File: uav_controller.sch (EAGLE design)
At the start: 20 parts, among them IC1 PIC16F877SO, U1 L298, U2 L298, U3 LCD-16X28X2

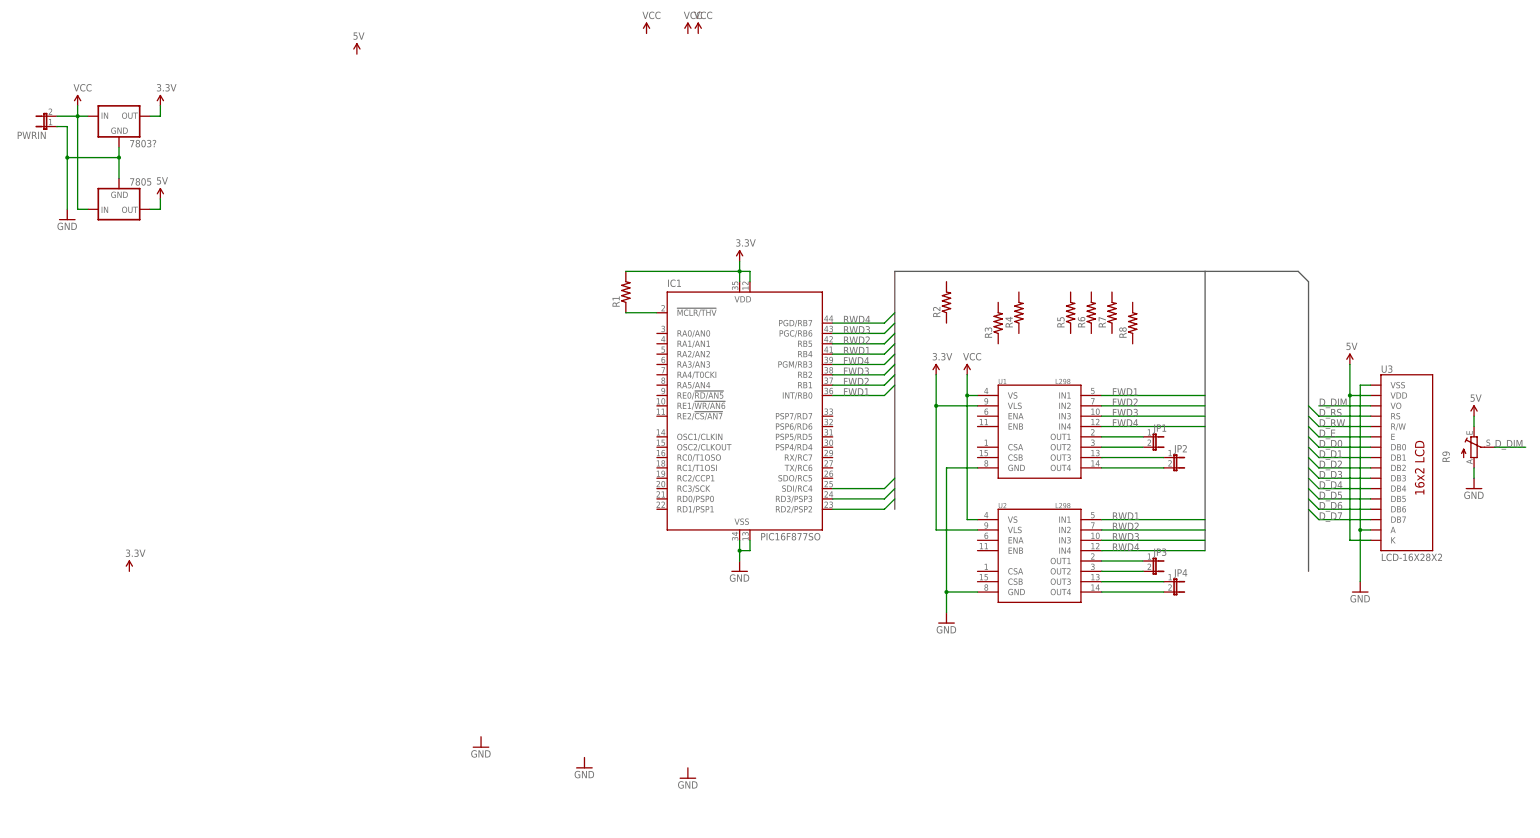
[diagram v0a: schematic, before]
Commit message: Added L3G4200D 3-Axis Gyro Carrier, not using the internal vreg. http://www.pololu.com/catalog/product/1272
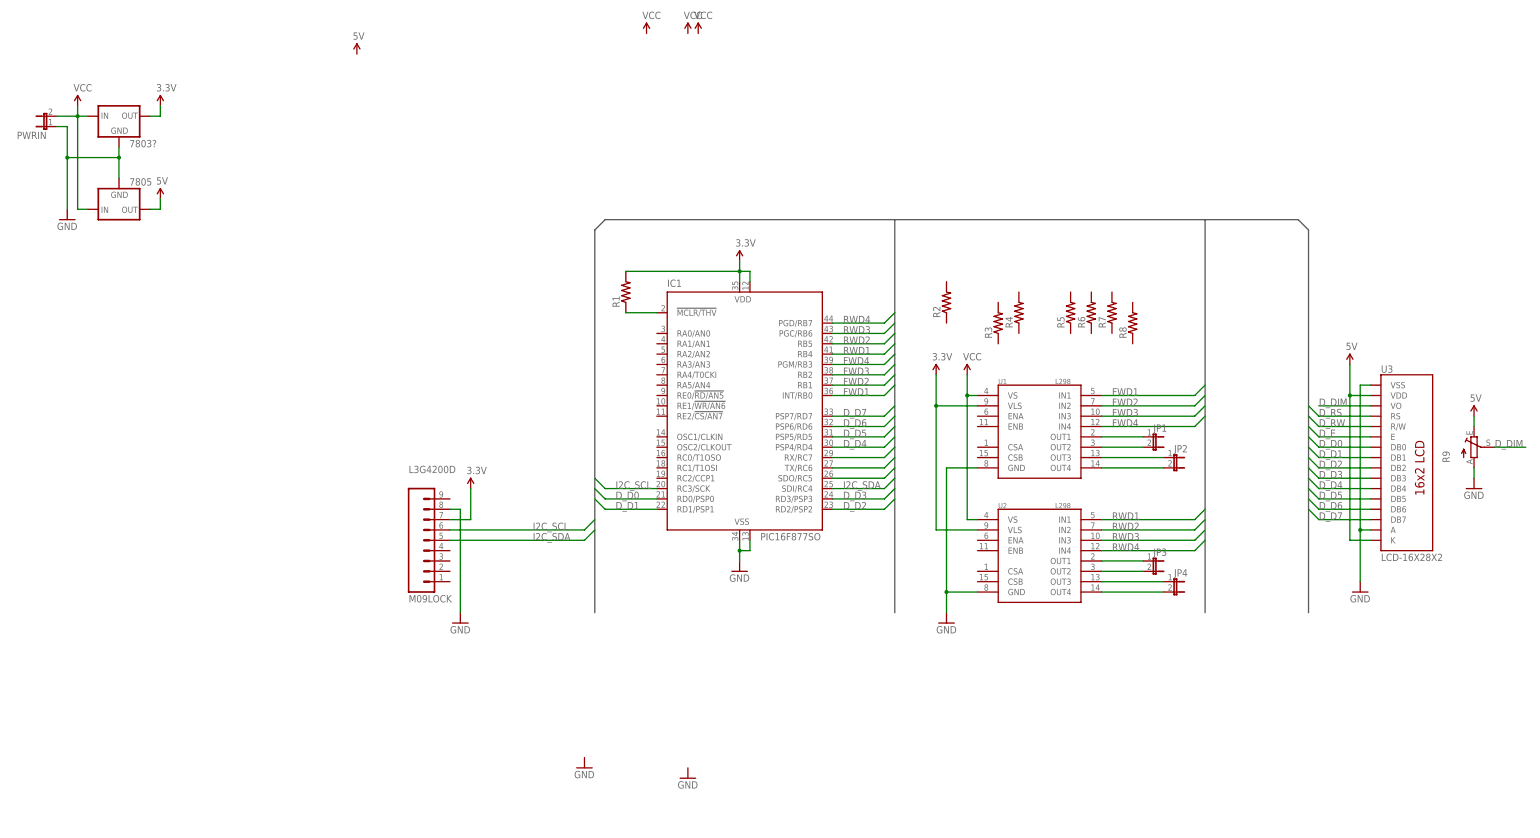
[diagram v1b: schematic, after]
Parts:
- added L3G4200D: M09LOCK, SparkFun-Connectors:M09LOCK
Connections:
- removed net N$19: IC1.RD2/PSP2
- removed net N$20: IC1.RD3/PSP3
- removed net N$21: IC1.SDI/RC4
- new net I2C_SCL: IC1.RC3/SCK, L3G4200D.6
- new net I2C_SDA: IC1.SDI/RC4, L3G4200D.5
- new net N$10: IC1.SDO/RC5
- new net N$11: IC1.TX/RC6
- new net N$12: IC1.RX/RC7
- net 3.3V: now also L3G4200D.7
- net D_D0: now also IC1.RD0/PSP0
- net D_D1: now also IC1.RD1/PSP1
- net D_D2: now also IC1.RD2/PSP2
- net D_D3: now also IC1.RD3/PSP3
- net D_D4: now also IC1.PSP4/RD4
- net D_D5: now also IC1.PSP5/RD5
- net D_D6: now also IC1.PSP6/RD6
- net D_D7: now also IC1.PSP7/RD7
- net GND: now also L3G4200D.8

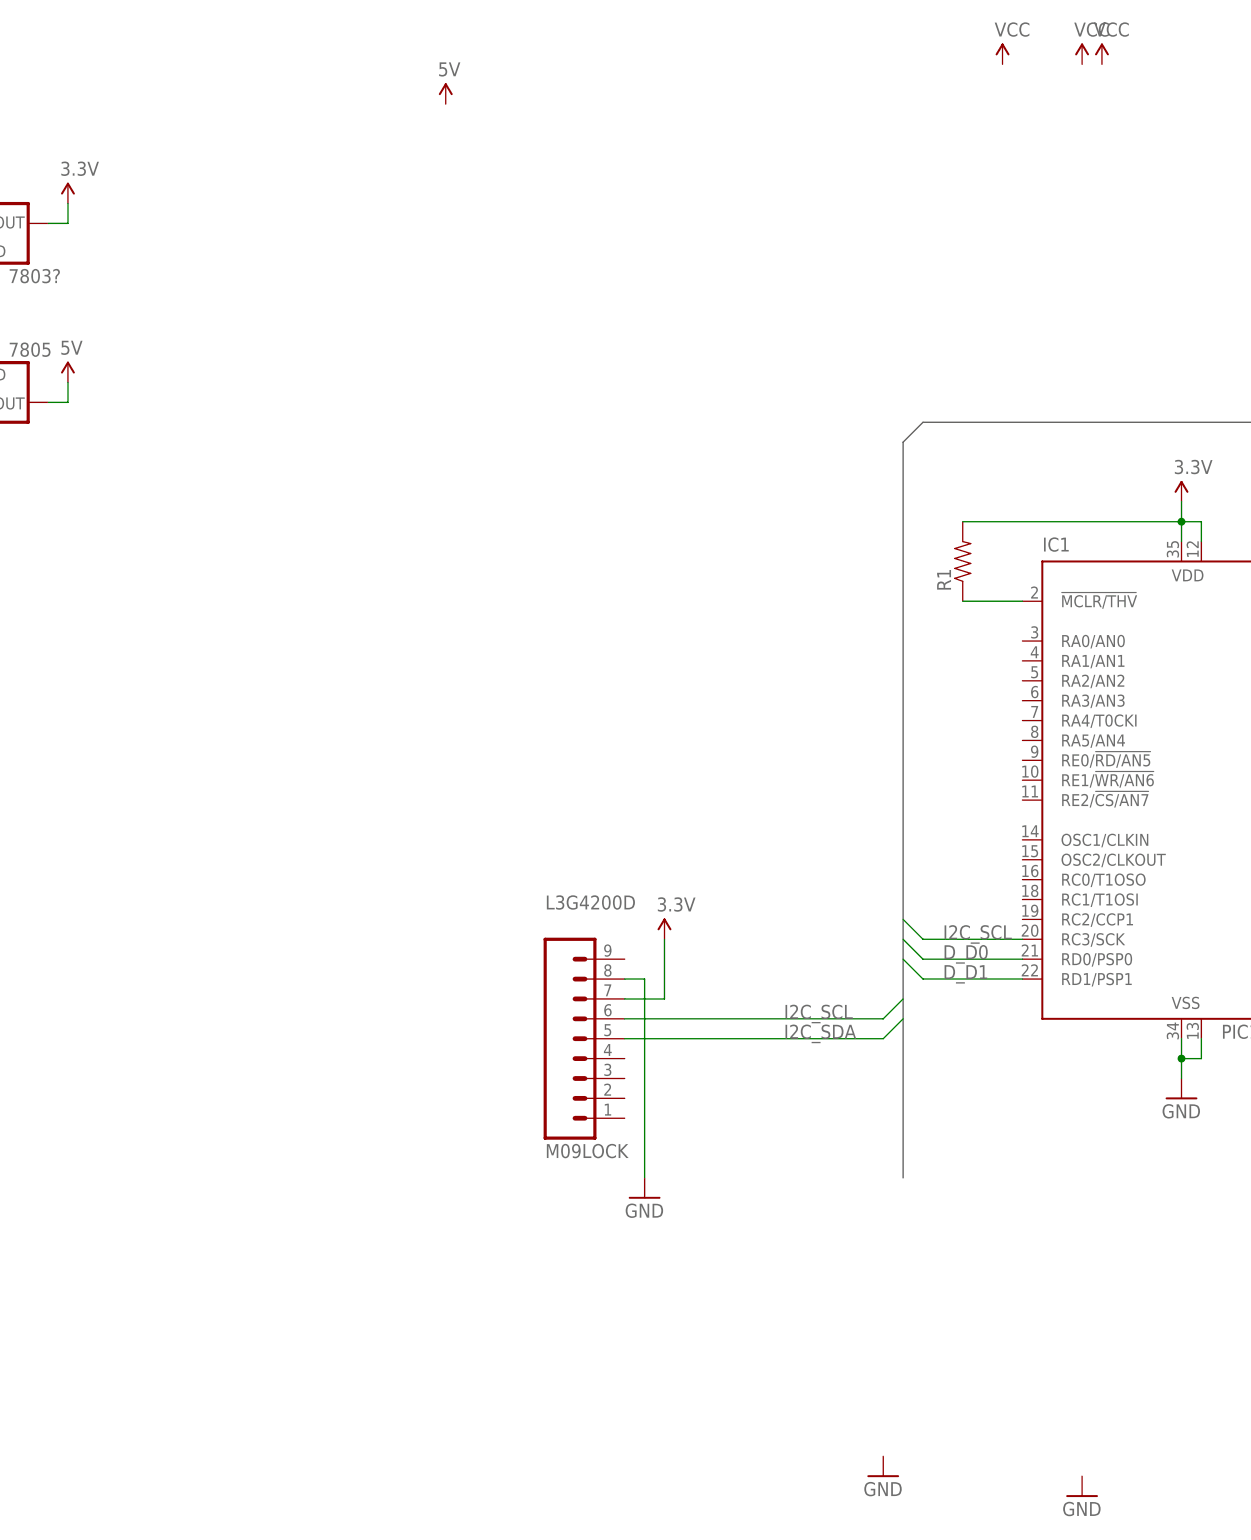
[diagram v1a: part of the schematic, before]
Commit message: Added OSC and connectors for analog range finders: http://www.pololu.com/catalog/product/136
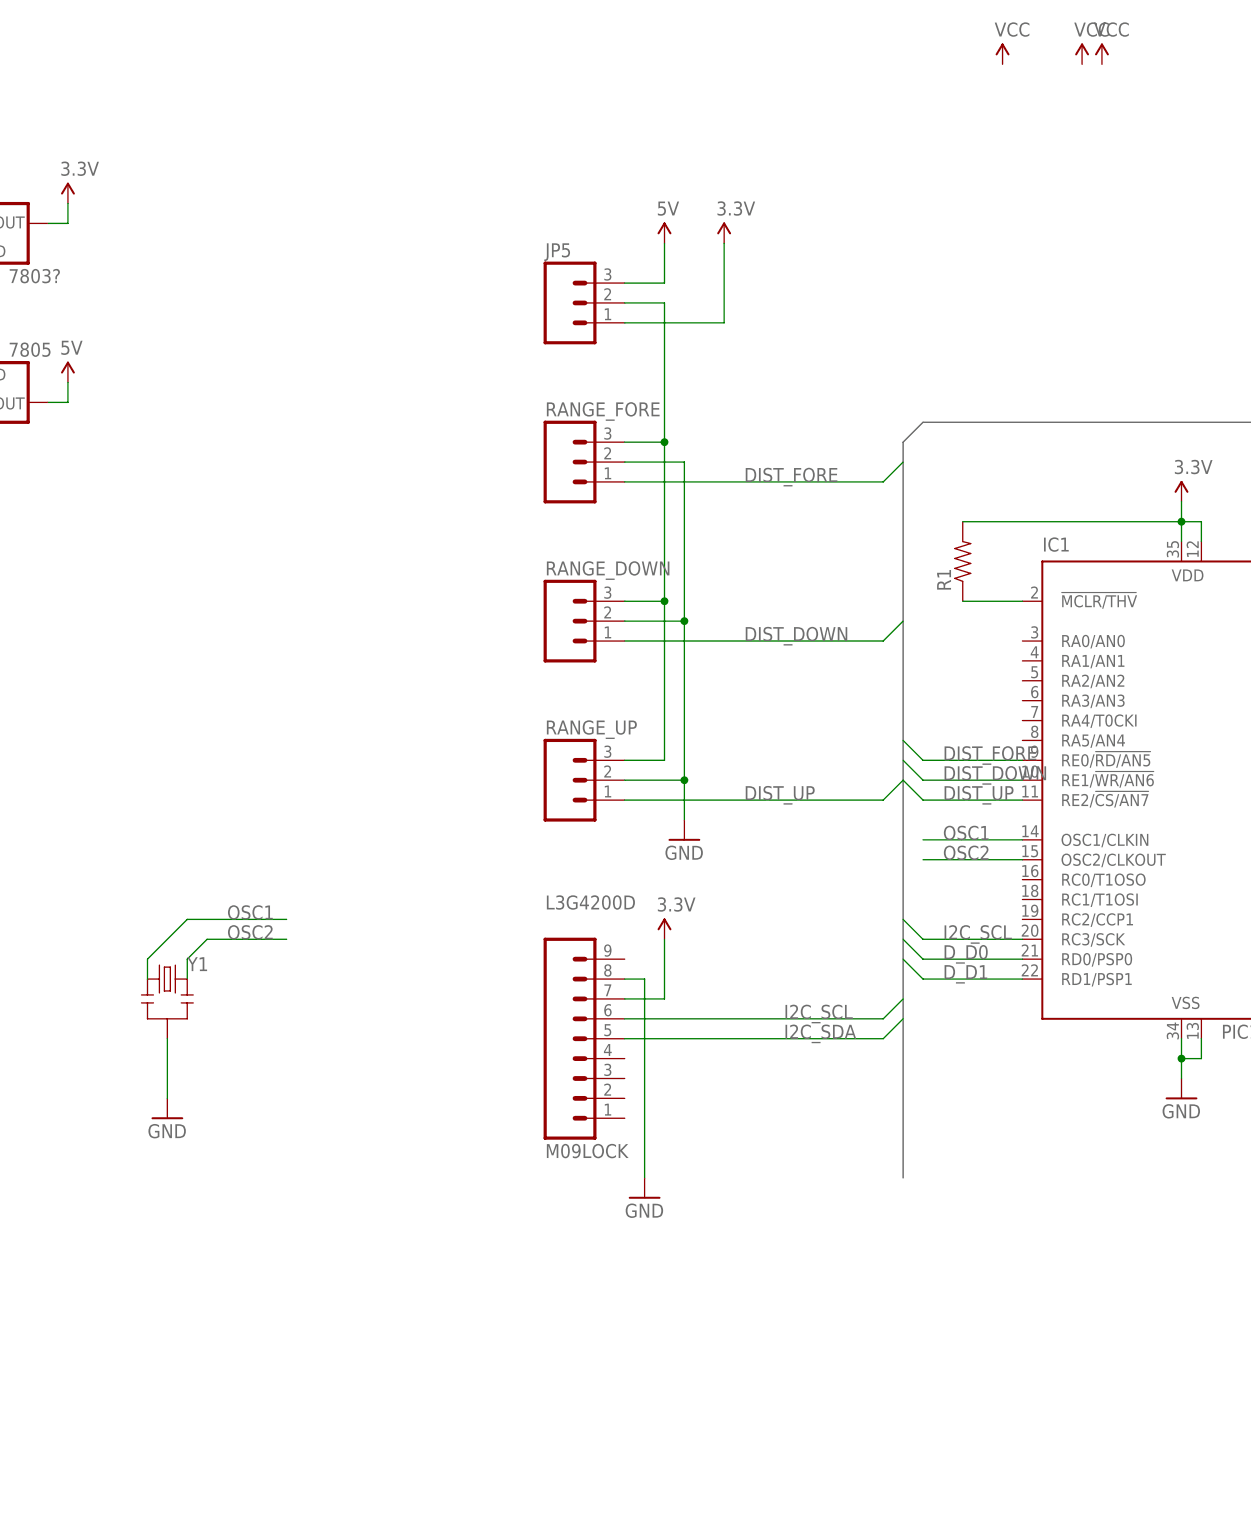
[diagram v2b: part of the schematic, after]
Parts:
- added JP5: (no value), SparkFun-Connectors:M03PTH
- added RANGE_DOWN, RANGE_FORE, RANGE_UP: (no value), SparkFun-Connectors:M03JST-PTH
- added Y1: (no value), SparkFun-FreqCtrl:RESONATORPTH
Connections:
- new net DIST_DOWN: IC1.RE1/!WR/AN6, RANGE_DOWN.1
- new net DIST_FORE: IC1.RE0/!RD/AN5, RANGE_FORE.1
- new net DIST_UP: IC1.RE2/!CS/AN7, RANGE_UP.1
- new net N$17: JP5.2, RANGE_DOWN.3, RANGE_FORE.3, RANGE_UP.3
- new net OSC1: IC1.OSC1/CLKIN, Y1.1
- new net OSC2: IC1.OSC2/CLKOUT, Y1.3
- net 3.3V: now also JP5.1
- net 5V: now also JP5.3
- net GND: now also RANGE_DOWN.2, RANGE_FORE.2, RANGE_UP.2, Y1.2
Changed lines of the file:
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@@
 <part name="GND8" library="SparkFun-Aesthetics" deviceset="GND" device=""/>
 <part name="L3G4200D" library="SparkFun-Connectors" deviceset="M09" device="LOCK"/>
+<part name="RANGE_UP" library="SparkFun-Connectors" deviceset="M03" device="JST-PTH"/>
+<part name="RANGE_DOWN" library="SparkFun-Connectors" deviceset="M03" device="JST-PTH"/>
+<part name="RANGE_FORE" library="SparkFun-Connectors" deviceset="M03" device="JST-PTH"/>
+<part name="JP5" library="SparkFun-Connectors" deviceset="M03" device="PTH"/>
+<part name="SUPPLY14" library="SparkFun-Aesthetics" deviceset="3.3V" device=""/>
+<part name="Y1" library="SparkFun-FreqCtrl" deviceset="RESONATOR" device="PTH"/>
 </parts>
 <sheets>
@@
 <instance part="SUPPLY10" gate="G$1" x="43.18" y="185.42"/>
 <instance part="SUPPLY11" gate="G$1" x="335.28" y="144.78"/>
-<instance part="SUPPLY12" gate="G$1" x="91.44" y="220.98"/>
+<instance part="SUPPLY12" gate="G$1" x="119.38" y="203.2"/>
 <instance part="SUPPLY13" gate="G$1" x="365.76" y="132.08"/>
 <instance part="R9" gate="1" x="365.76" y="124.46"/>
 <instance part="GND5" gate="1" x="116.84" y="81.28"/>
-<instance part="GND6" gate="1" x="147.32" y="45.72"/>
-<instance part="GND7" gate="1" x="172.72" y="43.18"/>
+<instance part="GND6" gate="1" x="121.92" y="127"/>
+<instance part="GND7" gate="1" x="55.88" y="91.44"/>
 <instance part="GND8" gate="1" x="365.76" y="114.3"/>
 <instance part="L3G4200D" gate="G$1" x="104.14" y="101.6"/>
+<instance part="RANGE_UP" gate="G$1" x="106.68" y="134.62"/>
+<instance part="RANGE_DOWN" gate="G$1" x="106.68" y="154.94"/>
+<instance part="RANGE_FORE" gate="G$1" x="106.68" y="175.26"/>
+<instance part="JP5" gate="G$1" x="106.68" y="195.58"/>
+<instance part="SUPPLY14" gate="G$1" x="127" y="203.2"/>
+<instance part="Y1" gate="G$1" x="55.88" y="109.22"/>
 </instances>
 <busses>
@@
 <pinref part="GND5" gate="1" pin="GND"/>
 </segment>
+<segment>
+<pinref part="RANGE_UP" gate="G$1" pin="2"/>
+<wire x1="114.3" y1="134.62" x2="121.92" y2="134.62" width="0.1524" layer="91"/>
+<pinref part="GND6" gate="1" pin="GND"/>
+<wire x1="121.92" y1="134.62" x2="121.92" y2="129.54" width="0.1524" layer="91"/>
+<wire x1="121.92" y1="134.62" x2="121.92" y2="154.94" width="0.1524" layer="91"/>
+<pinref part="RANGE_DOWN" gate="G$1" pin="2"/>
+<wire x1="121.92" y1="154.94" x2="114.3" y2="154.94" width="0.1524" layer="91"/>
+<wire x1="121.92" y1="154.94" x2="121.92" y2="175.26" width="0.1524" layer="91"/>
+<pinref part="RANGE_FORE" gate="G$1" pin="2"/>
+<wire x1="121.92" y1="175.26" x2="114.3" y2="175.26" width="0.1524" layer="91"/>
+<junction x="121.92" y="154.94"/>
+<junction x="121.92" y="134.62"/>
+</segment>
+<segment>
+<pinref part="GND7" gate="1" pin="GND"/>
+<pinref part="Y1" gate="G$1" pin="2"/>
+<wire x1="55.88" y1="93.98" x2="55.88" y2="101.6" width="0.1524" layer="91"/>
+</segment>
 </net>
 <net name="3.3V" class="0">
@@
 <wire x1="119.38" y1="106.68" x2="119.38" y2="114.3" width="0.1524" layer="91"/>
 </segment>
+<segment>
+<pinref part="SUPPLY14" gate="G$1" pin="3.3V"/>
+<wire x1="127" y1="203.2" x2="127" y2="193.04" width="0.1524" layer="91"/>
+<pinref part="JP5" gate="G$1" pin="1"/>
+<wire x1="127" y1="193.04" x2="114.3" y2="193.04" width="0.1524" layer="91"/>
+</segment>
 </net>
 <net name="VCC" class="0">
@@
 <wire x1="365.76" y1="132.08" x2="365.76" y2="129.54" width="0.1524" layer="91"/>
 </segment>
+<segment>
+<pinref part="JP5" gate="G$1" pin="3"/>
+<wire x1="114.3" y1="198.12" x2="119.38" y2="198.12" width="0.1524" layer="91"/>
+<pinref part="SUPPLY12" gate="G$1" pin="5V"/>
+<wire x1="119.38" y1="198.12" x2="119.38" y2="203.2" width="0.1524" layer="91"/>
+</segment>
 </net>
 <net name="D_DIM" class="0">
@@
 </segment>
 </net>
+<net name="DIST_UP" class="0">
+<segment>
+<pinref part="RANGE_UP" gate="G$1" pin="1"/>
+<wire x1="114.3" y1="132.08" x2="147.32" y2="132.08" width="0.1524" layer="91"/>
+<wire x1="147.32" y1="132.08" x2="149.86" y2="134.62" width="0.1524" layer="91"/>
+<label x="129.54" y="132.08" size="1.778" layer="95"/>
+<pinref part="IC1" gate="G$1" pin="RE2/!CS/AN7"/>
+<wire x1="165.1" y1="132.08" x2="152.4" y2="132.08" width="0.1524" layer="91"/>
+<wire x1="152.4" y1="132.08" x2="149.86" y2="134.62" width="0.1524" layer="91"/>
+<label x="154.94" y="132.08" size="1.778" layer="95"/>
+</segment>
+</net>
+<net name="DIST_DOWN" class="0">
+<segment>
+<pinref part="RANGE_DOWN" gate="G$1" pin="1"/>
+<wire x1="114.3" y1="152.4" x2="147.32" y2="152.4" width="0.1524" layer="91"/>
+<wire x1="147.32" y1="152.4" x2="149.86" y2="154.94" width="0.1524" layer="91"/>
+<label x="129.54" y="152.4" size="1.778" layer="95"/>
+</segment>
+<segment>
+<wire x1="149.86" y1="137.16" x2="152.4" y2="134.62" width="0.1524" layer="91"/>
+<pinref part="IC1" gate="G$1" pin="RE1/!WR/AN6"/>
+<wire x1="152.4" y1="134.62" x2="165.1" y2="134.62" width="0.1524" layer="91"/>
+<label x="154.94" y="134.62" size="1.778" layer="95"/>
+</segment>
+</net>
+<net name="DIST_FORE" class="0">
+<segment>
+<pinref part="RANGE_FORE" gate="G$1" pin="1"/>
+<wire x1="114.3" y1="172.72" x2="147.32" y2="172.72" width="0.1524" layer="91"/>
+<wire x1="147.32" y1="172.72" x2="149.86" y2="175.26" width="0.1524" layer="91"/>
+<label x="129.54" y="172.72" size="1.778" layer="95"/>
+</segment>
+<segment>
+<pinref part="IC1" gate="G$1" pin="RE0/!RD/AN5"/>
+<wire x1="165.1" y1="137.16" x2="152.4" y2="137.16" width="0.1524" layer="91"/>
+<wire x1="152.4" y1="137.16" x2="149.86" y2="139.7" width="0.1524" layer="91"/>
+<label x="154.94" y="137.16" size="1.778" layer="95"/>
+</segment>
+</net>
+<net name="N$17" class="0">
+<segment>
+<pinref part="JP5" gate="G$1" pin="2"/>
+<wire x1="114.3" y1="195.58" x2="119.38" y2="195.58" width="0.1524" layer="91"/>
+<wire x1="119.38" y1="195.58" x2="119.38" y2="177.8" width="0.1524" layer="91"/>
+<pinref part="RANGE_FORE" gate="G$1" pin="3"/>
+<wire x1="114.3" y1="177.8" x2="119.38" y2="177.8" width="0.1524" layer="91"/>
+<wire x1="119.38" y1="177.8" x2="119.38" y2="157.48" width="0.1524" layer="91"/>
+<pinref part="RANGE_DOWN" gate="G$1" pin="3"/>
+<wire x1="114.3" y1="157.48" x2="119.38" y2="157.48" width="0.1524" layer="91"/>
+<wire x1="119.38" y1="157.48" x2="119.38" y2="137.16" width="0.1524" layer="91"/>
+<pinref part="RANGE_UP" gate="G$1" pin="3"/>
+<wire x1="119.38" y1="137.16" x2="114.3" y2="137.16" width="0.1524" layer="91"/>
+<junction x="119.38" y="157.48"/>
+<junction x="119.38" y="177.8"/>
+</segment>
+</net>
+<net name="OSC2" class="0">
+<segment>
+<pinref part="Y1" gate="G$1" pin="3"/>
+<wire x1="58.42" y1="109.22" x2="58.42" y2="111.76" width="0.1524" layer="91"/>
+<wire x1="58.42" y1="111.76" x2="60.96" y2="114.3" width="0.1524" layer="91"/>
+<wire x1="60.96" y1="114.3" x2="71.12" y2="114.3" width="0.1524" layer="91"/>
+<label x="63.5" y="114.3" size="1.778" layer="95"/>
+</segment>
+<segment>
+<pinref part="IC1" gate="G$1" pin="OSC2/CLKOUT"/>
+<wire x1="165.1" y1="124.46" x2="152.4" y2="124.46" width="0.1524" layer="91"/>
+<label x="154.94" y="124.46" size="1.778" layer="95"/>
+</segment>
+</net>
+<net name="OSC1" class="0">
+<segment>
+<pinref part="Y1" gate="G$1" pin="1"/>
+<wire x1="53.34" y1="109.22" x2="53.34" y2="111.76" width="0.1524" layer="91"/>
+<wire x1="53.34" y1="111.76" x2="58.42" y2="116.84" width="0.1524" layer="91"/>
+<wire x1="58.42" y1="116.84" x2="71.12" y2="116.84" width="0.1524" layer="91"/>
+<label x="63.5" y="116.84" size="1.778" layer="95"/>
+</segment>
+<segment>
+<pinref part="IC1" gate="G$1" pin="OSC1/CLKIN"/>
+<wire x1="152.4" y1="127" x2="165.1" y2="127" width="0.1524" layer="91"/>
+<label x="154.94" y="127" size="1.778" layer="95"/>
+</segment>
+</net>

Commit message: Renamed some components
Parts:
- removed R2, R3, R4, R5, R6, R7, R8: (no value), SparkFun-Resistors:RESISTOREZ
- OSC: value (none) -> 8Mhz
- renumbered R9 to BKLT, U1 to HBRIDGE-FRONT, U2 to HBRIDGE-REAR, Y1 to OSC
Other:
- moved on the sheet: 7803?, 7805, PWRIN
